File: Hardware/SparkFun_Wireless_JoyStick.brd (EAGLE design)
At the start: 101.6 x 50.8 mm, 76 parts, among them J7 CORTEX_DEBUGPTH, Q1 2.5A/30V, U1 JOYSTICKPTH, U2 JOYSTICKPTH, U3 74AHC1G125, U4 AP2112K-3.3V, U5 XBEE-2B3, U6 MAX1704X, U7 MCP73831, U8 ATSAMD21G-A, Y1 32.768kHz

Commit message: Minor Changes
Too minor to mention
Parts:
- moved TP4 1.27 mm to (48.3, 33.0)
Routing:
- net !RESET: track 23.8 -> 22.5 mm
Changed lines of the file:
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@@
 <layer number="20" name="Dimension" color="15" fill="1" visible="yes" active="yes"/>
 <layer number="21" name="tPlace" color="16" fill="1" visible="yes" active="yes"/>
-<layer number="22" name="bPlace" color="14" fill="1" visible="no" active="yes"/>
+<layer number="22" name="bPlace" color="14" fill="1" visible="yes" active="yes"/>
 <layer number="23" name="tOrigins" color="15" fill="1" visible="yes" active="yes"/>
-<layer number="24" name="bOrigins" color="15" fill="1" visible="no" active="yes"/>
-<layer number="25" name="tNames" color="7" fill="1" visible="yes" active="yes"/>
+<layer number="24" name="bOrigins" color="15" fill="1" visible="yes" active="yes"/>
+<layer number="25" name="tNames" color="7" fill="1" visible="no" active="yes"/>
 <layer number="26" name="bNames" color="7" fill="1" visible="no" active="yes"/>
 <layer number="27" name="tValues" color="7" fill="1" visible="no" active="yes"/>
@@
 <layer number="45" name="Holes" color="7" fill="1" visible="no" active="yes"/>
 <layer number="46" name="Milling" color="3" fill="1" visible="no" active="yes"/>
-<layer number="47" name="Measures" color="7" fill="1" visible="no" active="yes"/>
+<layer number="47" name="Measures" color="7" fill="1" visible="yes" active="yes"/>
 <layer number="48" name="Document" color="7" fill="1" visible="no" active="yes"/>
 <layer number="49" name="Reference" color="7" fill="1" visible="no" active="yes"/>
@@
 <element name="TP2" library="SparkFun-Passives" package="PAD.03X.03" value="" x="44.45" y="19.05"/>
 <element name="TP3" library="SparkFun-Passives" package="PAD.03X.03" value="" x="48.26" y="24.13"/>
-<element name="TP4" library="SparkFun-Passives" package="PAD.03X.03" value="" x="48.26" y="34.29"/>
+<element name="TP4" library="SparkFun-Passives" package="PAD.03X.03" value="" x="48.26" y="33.02"/>
 <element name="D5" library="SparkFun-LED" package="LED-0603" value="RED" x="38.1" y="48.895" rot="R90">
 <attribute name="PROD_ID" value="DIO-00819" x="34.29" y="45.085" size="1.778" layer="27" font="vector" ratio="15" rot="R90" display="off"/>
@@
 <wire x1="50.546" y1="30.099" x2="48.895" y2="31.75" width="0.254" layer="16"/>
 <contactref element="TP4" pad="P$1"/>
-<wire x1="48.895" y1="31.75" x2="48.895" y2="33.655" width="0.254" layer="1"/>
-<wire x1="48.895" y1="33.655" x2="48.26" y2="34.29" width="0.254" layer="1"/>
+<wire x1="48.895" y1="31.75" x2="48.895" y2="32.385" width="0.254" layer="1"/>
+<wire x1="48.895" y1="32.385" x2="48.26" y2="33.02" width="0.254" layer="1"/>
 </signal>
 <signal name="AREF">

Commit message: QC Issues Fixed
- TX_LED and RX_LED nets are now all 0.006" width
- Version number changed to v01
- IO connections use 3.3V and GND symbols instead of net labels
- Replaced VBAT net label in LiPo Fuel Gauge with PWR symbol
- Inductor PROD_ID updated to match SKU in Sparkle
- Moved JTAG test points to bottom copper
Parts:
- moved TP4 10.2 mm to (53.3, 24.1), flipped to the bottom
- moved TP2 6.35 mm to (48.3, 24.1), flipped to the bottom
- moved TP3 2.54 mm to (50.8, 24.1), flipped to the bottom
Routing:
- net SWCLK: track 17.0 -> 21.5 mm
- net SWDIO: track 14.3 -> 16.5 mm
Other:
- board text added: "v01"
- board text removed: "v10"
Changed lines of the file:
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@@
 <?xml version="1.0" encoding="utf-8"?>
 <!DOCTYPE eagle SYSTEM "eagle.dtd">
-<eagle version="7.5.0">
+<eagle version="7.6.0">
 <drawing>
 <settings>
@@
 <layer number="22" name="bPlace" color="14" fill="1" visible="yes" active="yes"/>
 <layer number="23" name="tOrigins" color="15" fill="1" visible="yes" active="yes"/>
-<layer number="24" name="bOrigins" color="15" fill="1" visible="yes" active="yes"/>
-<layer number="25" name="tNames" color="7" fill="1" visible="no" active="yes"/>
+<layer number="24" name="bOrigins" color="15" fill="1" visible="no" active="yes"/>
+<layer number="25" name="tNames" color="7" fill="1" visible="yes" active="yes"/>
 <layer number="26" name="bNames" color="7" fill="1" visible="no" active="yes"/>
 <layer number="27" name="tValues" color="7" fill="1" visible="no" active="yes"/>
@@
 <layer number="37" name="tTest" color="7" fill="1" visible="no" active="yes"/>
 <layer number="38" name="bTest" color="7" fill="1" visible="no" active="yes"/>
-<layer number="39" name="tKeepout" color="4" fill="11" visible="no" active="yes"/>
-<layer number="40" name="bKeepout" color="1" fill="11" visible="no" active="yes"/>
+<layer number="39" name="tKeepout" color="4" fill="11" visible="yes" active="yes"/>
+<layer number="40" name="bKeepout" color="1" fill="11" visible="yes" active="yes"/>
 <layer number="41" name="tRestrict" color="4" fill="10" visible="no" active="yes"/>
 <layer number="42" name="bRestrict" color="1" fill="10" visible="no" active="yes"/>
@@
 <layer number="45" name="Holes" color="7" fill="1" visible="no" active="yes"/>
 <layer number="46" name="Milling" color="3" fill="1" visible="no" active="yes"/>
-<layer number="47" name="Measures" color="7" fill="1" visible="yes" active="yes"/>
+<layer number="47" name="Measures" color="7" fill="1" visible="no" active="yes"/>
 <layer number="48" name="Document" color="7" fill="1" visible="no" active="yes"/>
 <layer number="49" name="Reference" color="7" fill="1" visible="no" active="yes"/>
@@
 <dimension x1="6.35" y1="6.35" x2="1.859871875" y2="1.859871875" x3="4.104934375" y3="4.1049375" textsize="1.6764" textratio="15" layer="47" dtype="radius" unit="inch"/>
 <text x="41.91" y="54.61" size="1.6764" layer="47" font="vector" ratio="15">Units in Inches</text>
-<text x="44.069" y="0.381" size="1.6764" layer="16" font="vector" ratio="15" rot="MR0">v10</text>
+<text x="44.069" y="0.381" size="1.6764" layer="16" font="vector" ratio="15" rot="MR0">v01</text>
 <text x="70.0278" y="8.128" size="0.8128" layer="21" font="vector" ratio="15">R_PROG</text>
 <text x="70.104" y="3.556" size="0.8128" layer="21" font="vector" ratio="15">500mA</text>
@@
 </element>
 <element name="L1" library="SparkFun-Passives" package="0603" value="FB - 30 Ohm" x="37.465" y="11.43">
-<attribute name="PROD_ID" value="RES-07859" x="37.465" y="11.43" size="1.778" layer="27" font="vector" ratio="15" display="off"/>
+<attribute name="PROD_ID" value="NDUC-07859" x="37.465" y="11.43" size="1.778" layer="27" font="vector" ratio="15" display="off"/>
 </element>
 <element name="C7" library="SparkFun-Capacitors" package="0603-CAP" value="0.1uF" x="37.465" y="13.462" rot="R180">
@@
 </element>
 <element name="TP1" library="SparkFun-Passives" package="PAD.03X.03" value="" x="40.64" y="12.7"/>
-<element name="TP2" library="SparkFun-Passives" package="PAD.03X.03" value="" x="44.45" y="19.05"/>
-<element name="TP3" library="SparkFun-Passives" package="PAD.03X.03" value="" x="48.26" y="24.13"/>
-<element name="TP4" library="SparkFun-Passives" package="PAD.03X.03" value="" x="48.26" y="33.02"/>
+<element name="TP2" library="SparkFun-Passives" package="PAD.03X.03" value="" x="48.26" y="24.13" rot="MR0"/>
+<element name="TP3" library="SparkFun-Passives" package="PAD.03X.03" value="" x="50.8" y="24.13" rot="MR0"/>
+<element name="TP4" library="SparkFun-Passives" package="PAD.03X.03" value="" x="53.34" y="24.13" rot="MR0"/>
 <element name="D5" library="SparkFun-LED" package="LED-0603" value="RED" x="38.1" y="48.895" rot="R90">
 <attribute name="PROD_ID" value="DIO-00819" x="34.29" y="45.085" size="1.778" layer="27" font="vector" ratio="15" rot="R90" display="off"/>
@@
 <contactref element="J7" pad="2"/>
 <contactref element="U8" pad="46"/>
-<wire x1="45.085" y1="17.907" x2="45.085" y2="19.05" width="0.254" layer="1"/>
-<wire x1="45.085" y1="19.05" x2="45.085" y2="23.003771875" width="0.254" layer="1"/>
+<wire x1="45.085" y1="17.907" x2="45.085" y2="23.003771875" width="0.254" layer="1"/>
 <wire x1="45.085" y1="23.003771875" x2="47.481228125" y2="25.4" width="0.254" layer="1"/>
 <wire x1="47.481228125" y1="25.4" x2="48.26" y2="25.4" width="0.254" layer="1"/>
@@
 <wire x1="48.895" y1="26.035" x2="48.895" y2="26.67" width="0.254" layer="1"/>
 <contactref element="TP2" pad="P$1"/>
-<wire x1="44.45" y1="19.05" x2="45.085" y2="19.05" width="0.254" layer="1"/>
+<wire x1="48.26" y1="24.13" x2="48.895" y2="24.765" width="0.254" layer="16"/>
+<wire x1="48.895" y1="24.765" x2="48.895" y2="26.67" width="0.254" layer="16"/>
 </signal>
 <signal name="SWCLK">
@@
 <wire x1="45.72" y1="17.907" x2="45.72" y2="22.662778125" width="0.254" layer="1"/>
 <wire x1="45.72" y1="22.662778125" x2="47.822221875" y2="24.765" width="0.254" layer="1"/>
-<wire x1="47.822221875" y1="24.765" x2="48.26" y2="24.765" width="0.254" layer="1"/>
 <wire x1="45.72" y1="17.907" x2="46.883" y2="16.744" width="0.254" layer="1"/>
 <wire x1="46.883" y1="16.744" x2="46.883" y2="15.553" width="0.254" layer="1"/>
@@
 <wire x1="49.4991875" y1="27.94" x2="48.895" y2="27.94" width="0.254" layer="1"/>
 <contactref element="TP3" pad="P$1"/>
-<wire x1="48.26" y1="24.13" x2="48.26" y2="24.765" width="0.254" layer="1"/>
-<wire x1="48.26" y1="24.765" x2="49.403" y2="24.765" width="0.254" layer="1"/>
+<wire x1="47.822221875" y1="24.765" x2="49.403" y2="24.765" width="0.254" layer="1"/>
+<wire x1="50.8" y1="24.13" x2="50.8" y2="26.862371875" width="0.254" layer="16"/>
+<wire x1="50.8" y1="26.862371875" x2="49.722371875" y2="27.94" width="0.254" layer="16"/>
+<wire x1="49.722371875" y1="27.94" x2="48.895" y2="27.94" width="0.254" layer="16"/>
 </signal>
 <signal name="!RESET">
@@
 <wire x1="51.054" y1="18.542" x2="52.07" y2="18.542" width="0.254" layer="1"/>
 <via x="52.07" y="18.542" extent="1-16" drill="0.381"/>
-<wire x1="52.07" y1="18.542" x2="50.546" y2="20.066" width="0.254" layer="16"/>
-<wire x1="50.546" y1="20.066" x2="50.546" y2="30.099" width="0.254" layer="16"/>
-<wire x1="50.546" y1="30.099" x2="48.895" y2="31.75" width="0.254" layer="16"/>
 <contactref element="TP4" pad="P$1"/>
-<wire x1="48.895" y1="31.75" x2="48.895" y2="32.385" width="0.254" layer="1"/>
-<wire x1="48.895" y1="32.385" x2="48.26" y2="33.02" width="0.254" layer="1"/>
+<wire x1="48.895" y1="31.75" x2="49.637346875" y2="31.75" width="0.254" layer="16"/>
+<wire x1="49.637346875" y1="31.75" x2="53.34" y2="28.047346875" width="0.254" layer="16"/>
+<wire x1="53.34" y1="28.047346875" x2="53.34" y2="24.13" width="0.254" layer="16"/>
+<wire x1="53.34" y1="24.13" x2="53.34" y2="19.812" width="0.254" layer="16"/>
+<wire x1="53.34" y1="19.812" x2="52.07" y2="18.542" width="0.254" layer="16"/>
 </signal>
 <signal name="AREF">

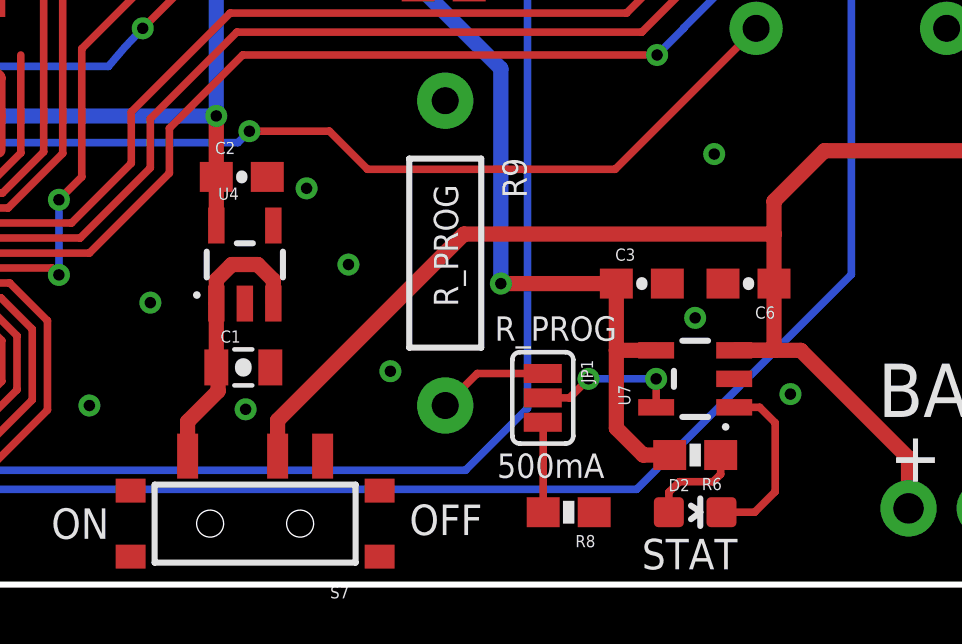
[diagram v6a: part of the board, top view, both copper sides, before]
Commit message: Proto Changes
- Added diode to allow powering the board from USB when no battery is
present.
- Switch now controls enable pin instead of VCC rail
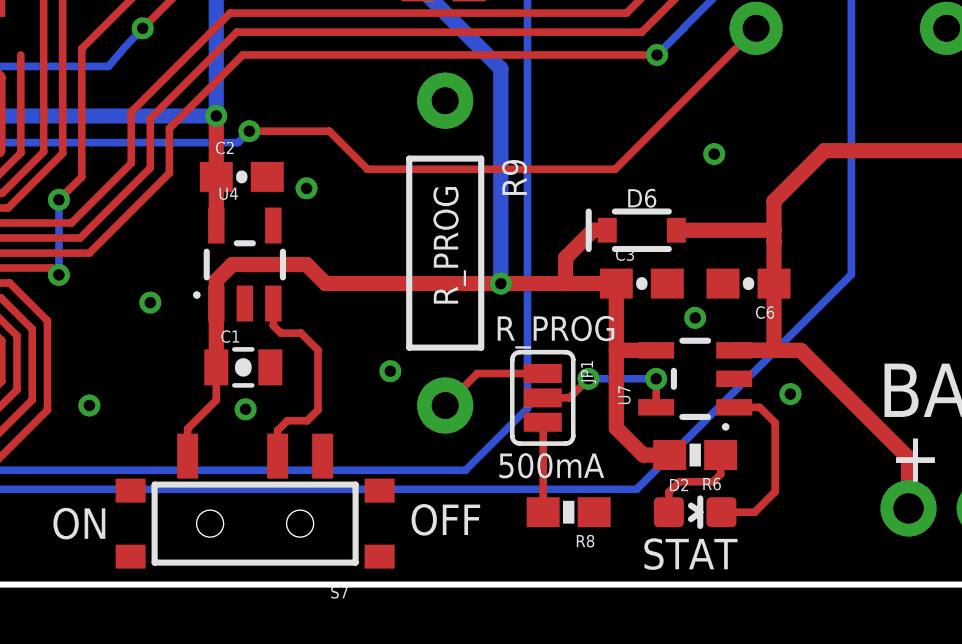
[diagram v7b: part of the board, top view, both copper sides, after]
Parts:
- added D6: 1A/23V/620mV, SparkFun-DiscreteSemi:SOD-323
- Q1: device SparkFun-DiscreteSemi:SOT23-3 -> SparkFun-DiscreteSemi:SOT23-3@1
- S7: value SWITCH_SPDT -> (none)
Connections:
- removed net VBAT_SW: C1.1, S7.O, U4.1, U4.3
- new net N$13: S7.P, U4.3
- net GND: now also S7.S
- net VBAT: now also D6.A; no longer S7.P
- net VIN: now also C1.1, D6.C, S7.O, U4.1
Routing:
- net VIN: track 54.2 -> 73.0 mm
- net VBAT: track 65.7 -> 48.7 mm
- net VBAT_SW: track 9.43 -> 0.00 mm
- net N$13: track 0.00 -> 7.04 mm
- net GND: vias 41 -> 40

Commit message: Updating version to 10
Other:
- board text added: "v10"
- board text removed: "v01"
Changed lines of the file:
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@@
 <layer number="37" name="tTest" color="7" fill="1" visible="no" active="yes"/>
 <layer number="38" name="bTest" color="7" fill="1" visible="no" active="yes"/>
-<layer number="39" name="tKeepout" color="4" fill="11" visible="yes" active="yes"/>
+<layer number="39" name="tKeepout" color="4" fill="11" visible="no" active="yes"/>
 <layer number="40" name="bKeepout" color="1" fill="11" visible="no" active="yes"/>
 <layer number="41" name="tRestrict" color="4" fill="10" visible="no" active="yes"/>
@@
 <dimension x1="6.35" y1="6.35" x2="1.859871875" y2="1.859871875" x3="4.104934375" y3="4.1049375" textsize="1.6764" textratio="15" layer="47" dtype="radius" unit="inch"/>
 <text x="41.91" y="54.61" size="1.6764" layer="47" font="vector" ratio="15">Units in Inches</text>
-<text x="44.069" y="0.381" size="1.6764" layer="16" font="vector" ratio="15" rot="MR0">v01</text>
+<text x="44.069" y="0.381" size="1.6764" layer="16" font="vector" ratio="15" rot="MR0">v10</text>
 <text x="70.0278" y="8.128" size="0.8128" layer="21" font="vector" ratio="15">R_PROG</text>
 <text x="70.104" y="3.556" size="0.8128" layer="21" font="vector" ratio="15">500mA</text>
